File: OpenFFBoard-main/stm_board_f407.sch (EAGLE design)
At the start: 51 parts, among them J1 10118193-0001LF, SW1 TL3342F160QG/TR, SW2 TL3342F160QG/TR, U1 STM32(LQFP64), X1 8MHz

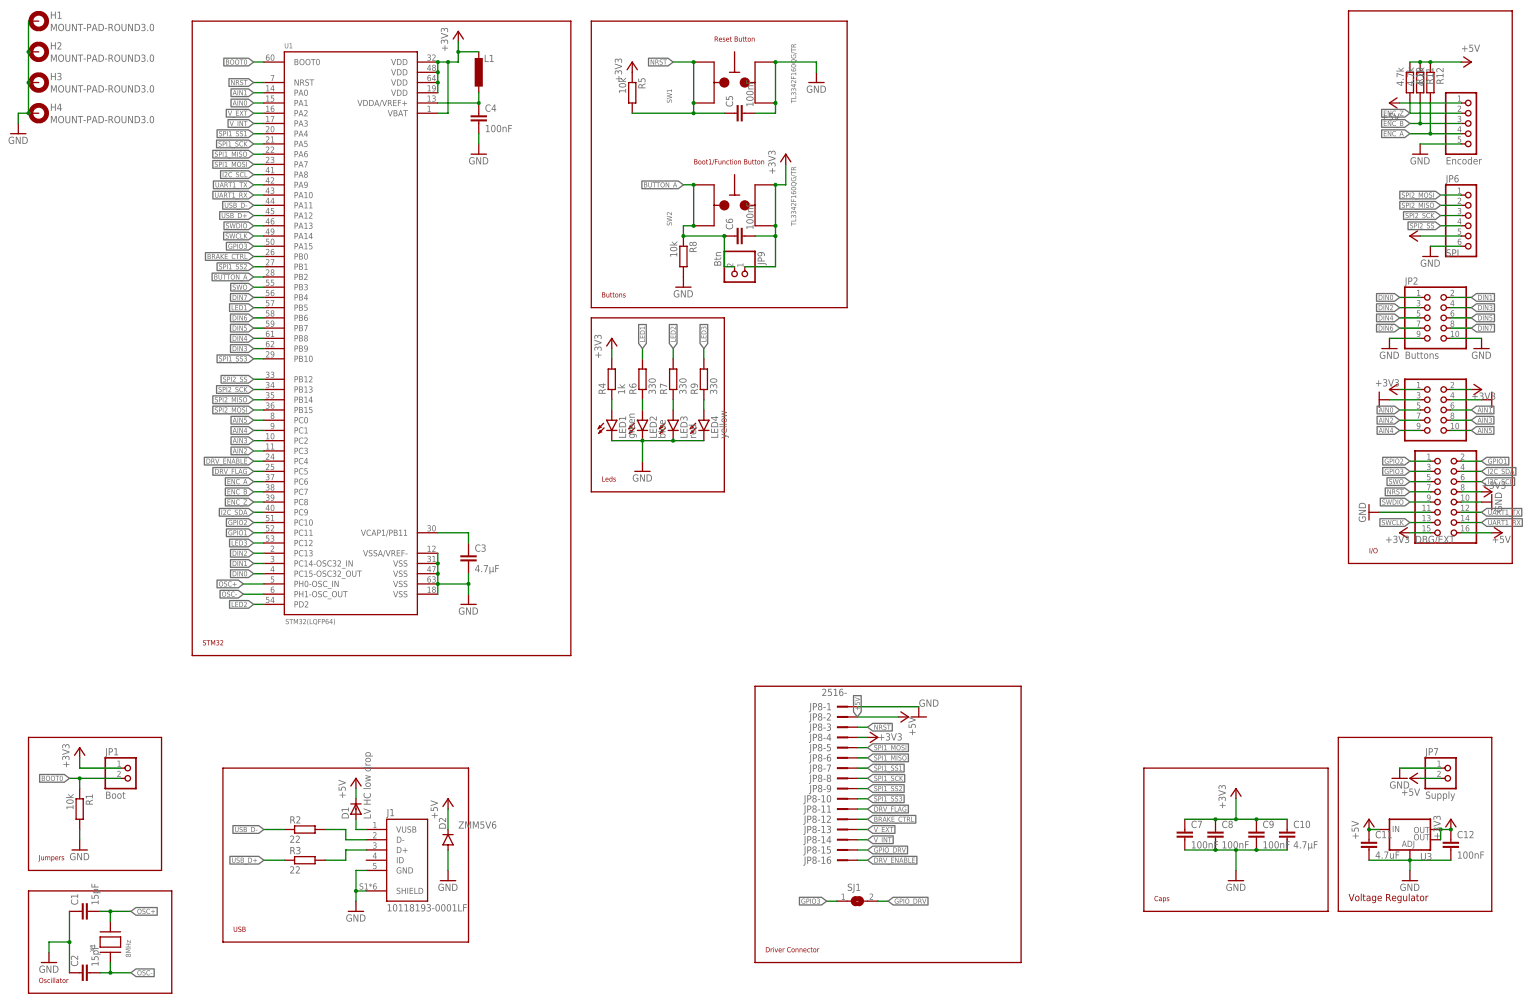
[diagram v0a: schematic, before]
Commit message: Updated STM Board to v1.2
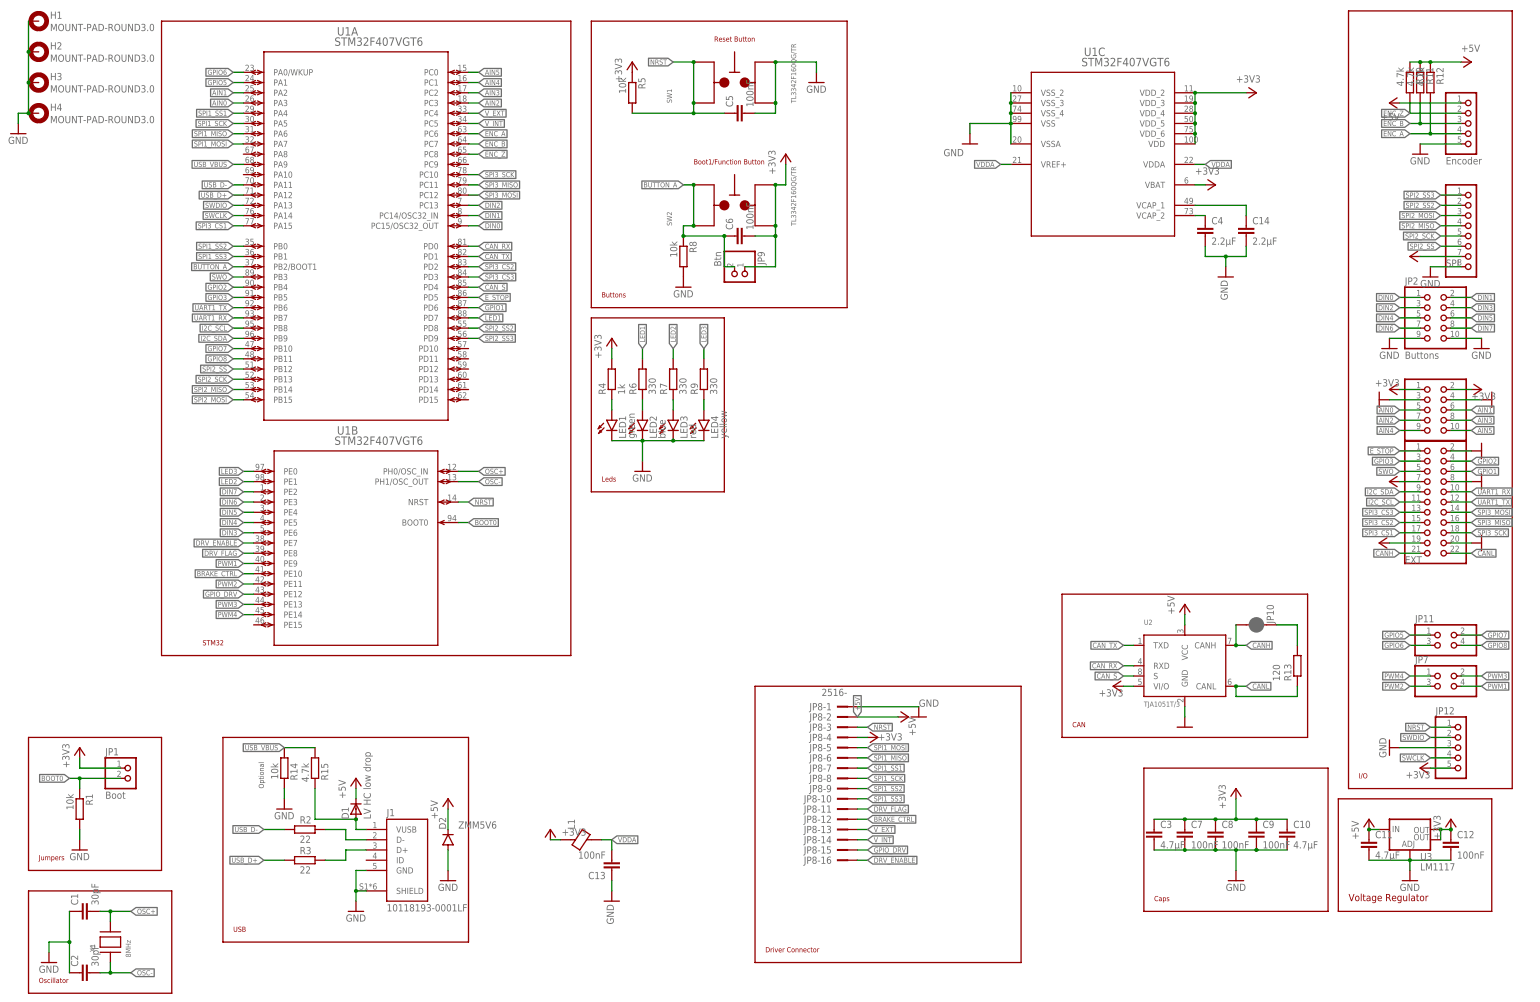
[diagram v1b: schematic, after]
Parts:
- removed SJ1: (no value), jumper:SJ
- added C13: 100nF, resistor:C-EUC0603
- added C14: 2.2µF, resistor:C-EUC0603
- added JP10: JUMPER-SMT_2_NC_PASTE_NO-SILK, SparkFun-Jumpers:JUMPER-SMT_2_NC_PASTE_NO-SILK
- added JP11: (no value), pinhead:PINHD-2X2
- added JP12: (no value), pinhead:PINHD-1X5
- added R13: 120, resistor:R-EU_R0603
- added R14: 10k, resistor:R-EU_R0603
- added R15: 4.7k, resistor:R-EU_R0603
- added U2: TJA1051T/3, TJA1051T_3:TJA1051T/3
- C1, C2: value 15pF -> 30pF
- C11: value 4.7uF -> 4.7µF
- C4: value 100nF -> 2.2µF
- JP4: value DBG/EXT -> EXT; device pinhead:PINHD-2X8 -> pinhead:PINHD-2X11
- JP6: device pinhead:PINHD-1X6 -> pinhead:PINHD-1X8
- JP7: value Supply -> (none); device pinhead:PINHD-1X2 -> pinhead:PINHD-2X2
- L1: value 2.2µH -> GZ2012D601TF; device resistor:L-EUL2012C -> Thermistor_Inductors:BLM21PG331SN1D
- LED1, LED2, LED3, LED4: device led:LEDCHIPLED_0805 -> led:LEDSML0805
- U1: value STM32(LQFP64) -> STM32F407VGT6; device STM32F411RET6:STM32(LQFP64) -> STM32:STM32F407VGT6
- U3: value (none) -> LM1117
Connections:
- new net CANH: JP10.2, JP4.21, U2.CANH
- new net CANL: JP4.22, R13.1, U2.CANL
- new net CAN_RX: U1A.PD0, U2.RXD
- new net CAN_S: U1A.PD4, U2.S
- new net CAN_TX: U1A.PD1, U2.TXD
- new net E_STOP: JP4.1, U1A.PD5
- new net GPIO5: JP11.1, U1A.PA1
- new net GPIO6: JP11.3, U1A.PA0/WKUP
- new net GPIO7: JP11.2, U1A.PB10
- new net GPIO8: JP11.4, U1A.PB11
- new net N$7: C4.1, U1C.VCAP_2
- new net PWM1: JP7.4, U1B.PE9
- new net PWM2: JP7.3, U1B.PE11
- new net PWM3: JP7.2, U1B.PE13
- new net PWM4: JP7.1, U1B.PE14
- new net SPI2_SS2: JP6.2, U1A.PD8
- new net SPI2_SS3: JP6.1, U1A.PD9
- new net SPI3_CS1: JP4.17, U1A.PA15
- new net SPI3_CS2: JP4.15, U1A.PD2
- new net SPI3_CS3: JP4.13, U1A.PD3
- new net SPI3_MISO: JP4.16, U1A.PC11
- new net SPI3_MOSI: JP4.14, U1A.PC12
- new net SPI3_SCK: JP4.18, U1A.PC10
- new net USB_VBUS: R14.1, R15.1, U1A.PA9
- new net VDDA: C13.2, L1.2, U1C.VDDA, U1C.VREF+
- net +3V3: now also C3.1, JP12.5, JP4.7, JP6.7, U1C.VBAT, U1C.VDD, U1C.VDD_2, U1C.VDD_3, U1C.VDD_4, U1C.VDD_5, U1C.VDD_6, U2.VI/O; no longer JP4.15, JP4.8, JP6.5, U1.VBAT, U1.VDD@1, U1.VDD@2, U1.VDD@3, U1.VDD@4
- net +5V: now also JP4.19, U2.VCC; no longer JP4.16, JP7.2
- net AIN0: now also U1A.PA3; no longer U1.PA1
- net AIN1: now also U1A.PA2; no longer U1.PA0
- net AIN2: now also U1A.PC3; no longer U1.PC3
- net AIN3: now also U1A.PC2; no longer U1.PC2
- net AIN4: now also U1A.PC1; no longer U1.PC1
- net AIN5: now also U1A.PC0; no longer U1.PC0
- net BOOT0: now also U1B.BOOT0; no longer U1.BOOT0
- net BRAKE_CTRL: now also U1B.PE10; no longer U1.PB0
- net BUTTON_A: now also U1A.PB2/BOOT1; no longer U1.PB2
- net DIN0: now also U1A.PC15/OSC32_OUT; no longer U1.PC15-OSC32_OUT
- net DIN1: now also U1A.PC14/OSC32_IN; no longer U1.PC14-OSC32_IN
- net DIN2: now also U1A.PC13; no longer U1.PC13
- net DIN3: now also U1B.PE6; no longer U1.PB9
- net DIN4: now also U1B.PE5; no longer U1.PB8
- net DIN5: now also U1B.PE4; no longer U1.PB7
- net DIN6: now also U1B.PE3; no longer U1.PB6
- net DIN7: now also U1B.PE2; no longer U1.PB4
- net DRV_ENABLE: now also U1B.PE7; no longer U1.PC4
- net DRV_FLAG: now also U1B.PE8; no longer U1.PC5
- net ENC_A: now also U1A.PC6; no longer U1.PC6
- net ENC_B: now also U1A.PC7; no longer U1.PC7
- net ENC_Z: now also U1A.PC8; no longer U1.PC8
- net GND: now also C13.1, C14.2, JP12.3, JP4.2, JP4.20, JP4.8, JP6.8, R14.2, U1C.VSS, U1C.VSSA, U1C.VSS_2, U1C.VSS_3, U1C.VSS_4, U2.GND; no longer JP4.10, JP4.11, JP6.6, JP7.1, U1.VSS@1, U1.VSS@2, U1.VSS@3, U1.VSS@4, U1.VSSA/VREF-
- net GPIO1: now also JP4.6, U1A.PD6; no longer JP4.2, U1.PC11
- net GPIO2: now also JP4.4, U1A.PB4; no longer JP4.1, U1.PC10
- net GPIO3: now also U1A.PB5; no longer SJ1.1, U1.PA15
- net GPIO_DRV: now also U1B.PE12; no longer SJ1.2
- net I2C_SCL: now also JP4.11, U1A.PB8; no longer JP4.6, U1.PA8
- net I2C_SDA: now also JP4.9, U1A.PB9; no longer JP4.4, U1.PC9
- net LED1: now also U1A.PD7; no longer U1.PB5
- net LED2: now also U1B.PE1; no longer U1.PD2
- net LED3: now also U1B.PE0; no longer U1.PC12
- net N$1: now also R15.2
- net N$3: now also JP10.1, R13.2; no longer C4.1, L1.2, U1.VDDA/VREF+
- net N$4: now also C14.1, U1C.VCAP_1; no longer C3.1, U1.VCAP1/PB11
- net NRST: now also JP12.1, U1B.NRST; no longer JP4.7, U1.NRST
- net OSC+: now also U1B.PH0/OSC_IN; no longer U1.PH0-OSC_IN
- net OSC-: now also U1B.PH1/OSC_OUT; no longer U1.PH1-OSC_OUT
- net SPI1_MISO: now also U1A.PA6; no longer U1.PA6
- net SPI1_MOSI: now also U1A.PA7; no longer U1.PA7
- net SPI1_SCK: now also U1A.PA5; no longer U1.PA5
- net SPI1_SS1: now also U1A.PA4; no longer U1.PA4
- net SPI1_SS2: now also U1A.PB0; no longer U1.PB1
- net SPI1_SS3: now also U1A.PB1; no longer U1.PB10
- net SPI2_MISO: now also JP6.4, U1A.PB14; no longer JP6.2, U1.PB14
- net SPI2_MOSI: now also JP6.3, U1A.PB15; no longer JP6.1, U1.PB15
- net SPI2_SCK: now also JP6.5, U1A.PB13; no longer JP6.3, U1.PB13
- net SPI2_SS: now also JP6.6, U1A.PB12; no longer JP6.4, U1.PB12
- net SWCLK: now also JP12.4, U1A.PA14; no longer JP4.13, U1.PA14
- net SWDIO: now also JP12.2, U1A.PA13; no longer JP4.9, U1.PA13
- net SWO: now also U1A.PB3; no longer U1.PB3
- net UART1_RX: now also JP4.10, U1A.PB7; no longer JP4.14, U1.PA10
- net UART1_TX: now also U1A.PB6; no longer U1.PA9
- net USB_D+: now also U1A.PA12; no longer U1.PA12
- net USB_D-: now also U1A.PA11; no longer U1.PA11
- net V_EXT: now also U1A.PC4; no longer U1.PA2
- net V_INT: now also U1A.PC5; no longer U1.PA3
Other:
- note added: "CAN"
- note added: "Optional"
- moved on the sheet: C3, C4

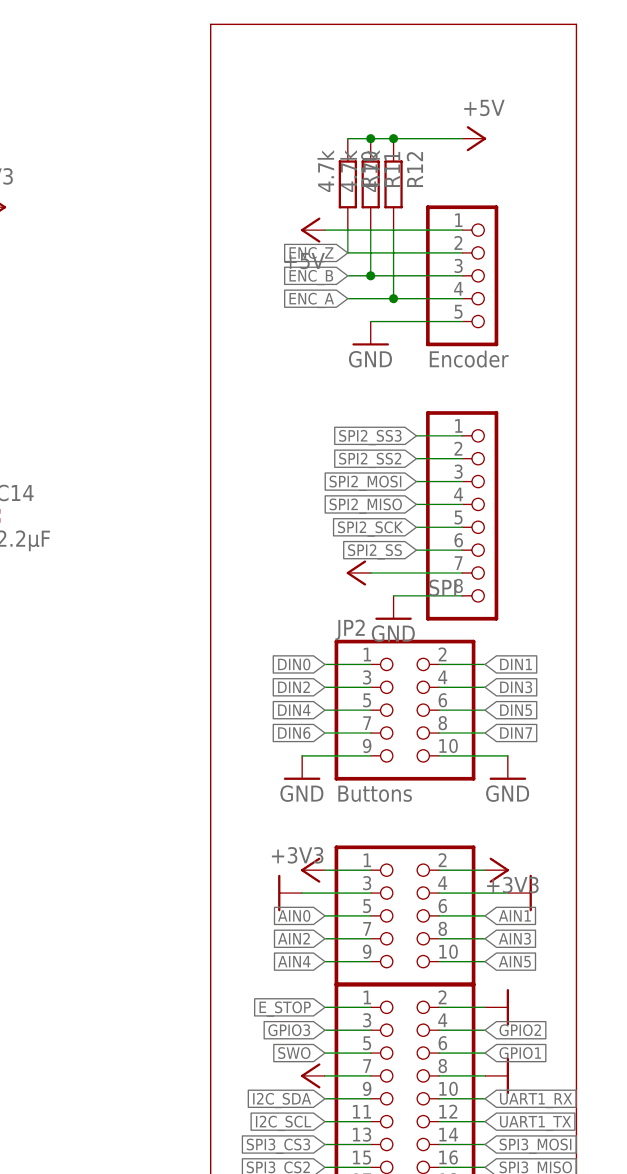
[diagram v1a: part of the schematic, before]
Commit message: Added E-Stop cap
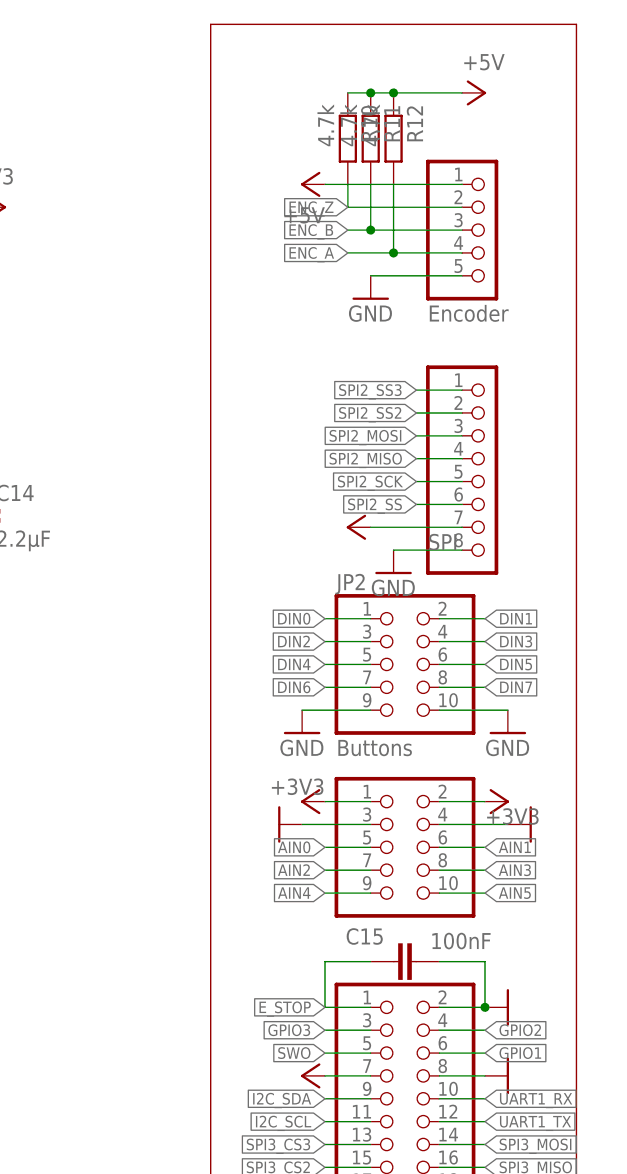
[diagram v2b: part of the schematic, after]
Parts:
- added C15: 100nF, resistor:C-EUC0603
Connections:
- net E_STOP: now also C15.1
- net GND: now also C15.2
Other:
- moved on the sheet: JP2, R10, R11, R12
